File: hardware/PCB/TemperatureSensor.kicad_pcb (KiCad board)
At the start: 2 copper layers, 2 parts, among them IC1 BQ24092DGQR, IC2 ESP32-D0WD-V3

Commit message: Add new sensors to board
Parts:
- added IC3: SHT31-ARP-B2.5kS, ProjectFootprints:SON50P250X250X100-9N-D, F.Cu at (36.8, 22.9)
- added U1: LTR-329ALS-01, ProjectFootprints:LTR329ALS01, F.Cu at (59.7, 21.6)
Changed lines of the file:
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@@
     (tracks 0)
     (zones 0)
-    (modules 2)
+    (modules 4)
     (nets 1)
   )
@@
     (add_net "Net-(IC2-Pad8)")
     (add_net "Net-(IC2-Pad9)")
+    (add_net "Net-(IC3-Pad1)")
+    (add_net "Net-(IC3-Pad2)")
+    (add_net "Net-(IC3-Pad3)")
+    (add_net "Net-(IC3-Pad4)")
+    (add_net "Net-(IC3-Pad5)")
+    (add_net "Net-(IC3-Pad6)")
+    (add_net "Net-(IC3-Pad7)")
+    (add_net "Net-(IC3-Pad8)")
+    (add_net "Net-(IC3-Pad9)")
+    (add_net "Net-(U1-Pad1)")
+    (add_net "Net-(U1-Pad2)")
+    (add_net "Net-(U1-Pad3)")
+    (add_net "Net-(U1-Pad4)")
+  )
+  (module ProjectFootprints:LTR329ALS01 (layer F.Cu)
+    (at 59.69 21.59)
+    (descr LTR-329ALS-01)
+    (tags "Undefined or Miscellaneous")
+    (attr smd)
+    (fp_text reference U1 (at 0 0) (layer F.SilkS)
+      (effects (font (size 1.27 1.27) (thickness 0.254)))
+    )
+    (fp_text value LTR-329ALS-01 (at 0 0) (layer F.SilkS) hide
+      (effects (font (size 1.27 1.27) (thickness 0.254)))
+    )
+    (fp_arc (start -0.7 1.225) (end -0.6 1.225) (angle 180) (layer F.SilkS) (width 0.2))
+    (fp_arc (start -0.7 1.225) (end -0.8 1.225) (angle 180) (layer F.SilkS) (width 0.2))
+    (fp_text user %R (at 0 0) (layer F.Fab)
+      (effects (font (size 1.27 1.27) (thickness 0.254)))
+    )
+    (fp_line (start -1 -1.275) (end 1 -1.275) (layer F.Fab) (width 0.2))
+    (fp_line (start 1 -1.275) (end 1 0.725) (layer F.Fab) (width 0.2))
+    (fp_line (start 1 0.725) (end -1 0.725) (layer F.Fab) (width 0.2))
+    (fp_line (start -1 0.725) (end -1 -1.275) (layer F.Fab) (width 0.2))
+    (fp_line (start -1.5 -1.825) (end 1.5 -1.825) (layer F.CrtYd) (width 0.1))
+    (fp_line (start 1.5 -1.825) (end 1.5 1.825) (layer F.CrtYd) (width 0.1))
+    (fp_line (start 1.5 1.825) (end -1.5 1.825) (layer F.CrtYd) (width 0.1))
+    (fp_line (start -1.5 1.825) (end -1.5 -1.825) (layer F.CrtYd) (width 0.1))
+    (fp_line (start -0.1 -1.275) (end 0.1 -1.275) (layer F.SilkS) (width 0.1))
+    (fp_line (start -1 -0.375) (end -1 -0.175) (layer F.SilkS) (width 0.1))
+    (fp_line (start 1 -0.375) (end 1 -0.175) (layer F.SilkS) (width 0.1))
+    (fp_line (start -0.1 0.725) (end 0.1 0.725) (layer F.SilkS) (width 0.1))
+    (fp_line (start -0.8 1.225) (end -0.8 1.225) (layer F.SilkS) (width 0.2))
+    (fp_line (start -0.6 1.225) (end -0.6 1.225) (layer F.SilkS) (width 0.2))
+    (pad 4 smd rect (at -0.6 -0.95) (size 0.7 0.75) (layers F.Cu F.Paste F.Mask))
+    (pad 3 smd rect (at 0.6 -0.95) (size 0.7 0.75) (layers F.Cu F.Paste F.Mask))
+    (pad 2 smd rect (at 0.6 0.4) (size 0.7 0.75) (layers F.Cu F.Paste F.Mask))
+    (pad 1 smd rect (at -0.6 0.4) (size 0.7 0.75) (layers F.Cu F.Paste F.Mask))
+  )
+  (module ProjectFootprints:SON50P250X250X100-9N-D (layer F.Cu)
+    (at 36.83 22.86)
+    (descr "8-DFN (2.5x2.5)")
+    (tags "Integrated Circuit")
+    (attr smd)
+    (fp_text reference IC3 (at 0 0) (layer F.SilkS)
+      (effects (font (size 1.27 1.27) (thickness 0.254)))
+    )
+    (fp_text value SHT31-ARP-B2.5kS (at 0 0) (layer F.SilkS) hide
+      (effects (font (size 1.27 1.27) (thickness 0.254)))
+    )
+    (fp_text user %R (at 0 0) (layer F.Fab)
+      (effects (font (size 1.27 1.27) (thickness 0.254)))
+    )
+    (fp_line (start -1.85 -1.55) (end 1.85 -1.55) (layer F.CrtYd) (width 0.05))
+    (fp_line (start 1.85 -1.55) (end 1.85 1.55) (layer F.CrtYd) (width 0.05))
+    (fp_line (start 1.85 1.55) (end -1.85 1.55) (layer F.CrtYd) (width 0.05))
+    (fp_line (start -1.85 1.55) (end -1.85 -1.55) (layer F.CrtYd) (width 0.05))
+    (fp_line (start -1.25 -1.25) (end 1.25 -1.25) (layer F.Fab) (width 0.1))
+    (fp_line (start 1.25 -1.25) (end 1.25 1.25) (layer F.Fab) (width 0.1))
+    (fp_line (start 1.25 1.25) (end -1.25 1.25) (layer F.Fab) (width 0.1))
+    (fp_line (start -1.25 1.25) (end -1.25 -1.25) (layer F.Fab) (width 0.1))
+    (fp_line (start -1.25 -0.625) (end -0.625 -1.25) (layer F.Fab) (width 0.1))
+    (fp_circle (center -1.6 -1.4) (end -1.6 -1.275) (layer F.SilkS) (width 0.25))
+    (pad 9 smd rect (at 0 0) (size 1.2 1.9) (layers F.Cu F.Paste F.Mask))
+    (pad 8 smd rect (at 1.2 -0.75 90) (size 0.3 0.8) (layers F.Cu F.Paste F.Mask))
+    (pad 7 smd rect (at 1.2 -0.25 90) (size 0.3 0.8) (layers F.Cu F.Paste F.Mask))
+    (pad 6 smd rect (at 1.2 0.25 90) (size 0.3 0.8) (layers F.Cu F.Paste F.Mask))
+    (pad 5 smd rect (at 1.2 0.75 90) (size 0.3 0.8) (layers F.Cu F.Paste F.Mask))
+    (pad 4 smd rect (at -1.2 0.75 90) (size 0.3 0.8) (layers F.Cu F.Paste F.Mask))
+    (pad 3 smd rect (at -1.2 0.25 90) (size 0.3 0.8) (layers F.Cu F.Paste F.Mask))
+    (pad 2 smd rect (at -1.2 -0.25 90) (size 0.3 0.8) (layers F.Cu F.Paste F.Mask))
+    (pad 1 smd rect (at -1.2 -0.75 90) (size 0.3 0.8) (layers F.Cu F.Paste F.Mask))
+    (model C:\Users\Pascal\Documents\Projects\WeatherStation\hardware\Library\SamacSys_Parts.3dshapes\SHT31-ARP-B2.5kS.stp
+      (at (xyz 0 0 0))
+      (scale (xyz 1 1 1))
+      (rotate (xyz 0 0 0))
+    )
   )
   (module ProjectFootprints:QFN35P500X500X90-49N-D (layer F.Cu)

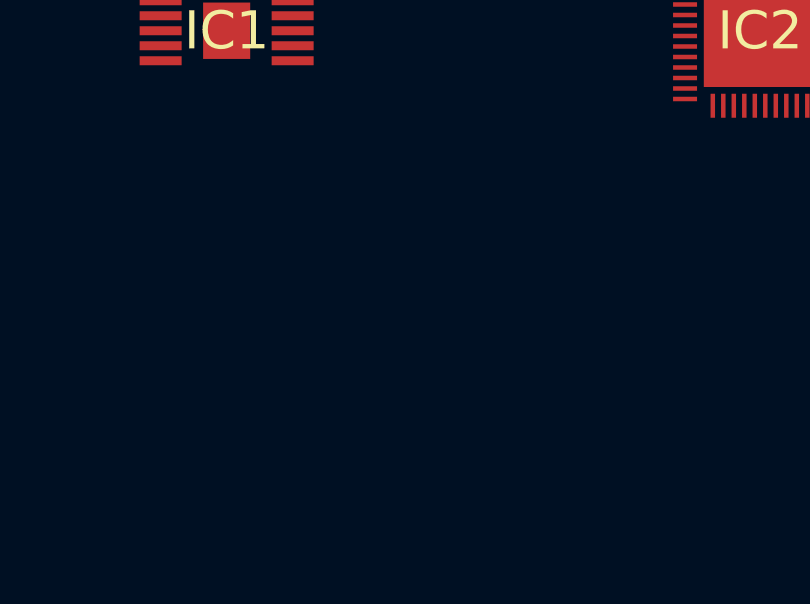
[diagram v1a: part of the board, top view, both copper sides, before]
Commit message: add usb and ftdi circuit
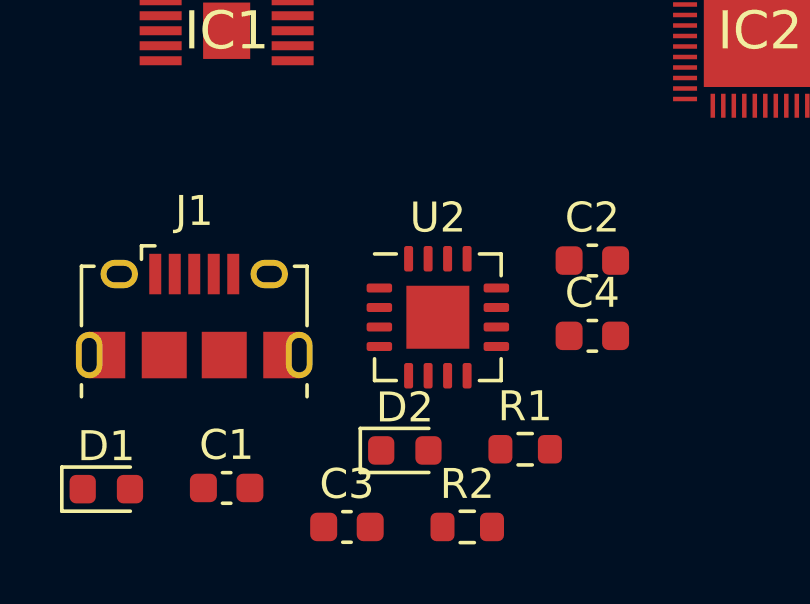
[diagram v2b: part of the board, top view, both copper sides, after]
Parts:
- added C1: 100n, Capacitor_SMD:C_0603_1608Metric, F.Cu at (31.8, 45.7)
- added C2: 4u7, Capacitor_SMD:C_0603_1608Metric, F.Cu at (43.9, 38.1)
- added C3: 100n, Capacitor_SMD:C_0603_1608Metric, F.Cu at (35.8, 47.0)
- added C4: 100n, Capacitor_SMD:C_0603_1608Metric, F.Cu at (43.9, 40.6)
- added D1: LED, LED_SMD:LED_0603_1608Metric, F.Cu at (27.7, 45.8)
- added D2: LED, LED_SMD:LED_0603_1608Metric, F.Cu at (37.7, 44.5)
- added J1: USB_B_Micro, Connector_USB:USB_Micro-B_Amphenol_10118194_Horizontal, F.Cu at (30.7, 40.0)
- added R1: 620R, Resistor_SMD:R_0603_1608Metric, F.Cu at (41.7, 44.4)
- added R2: 620R, Resistor_SMD:R_0603_1608Metric, F.Cu at (39.8, 47.0)
- added U2: FT230XQ, Package_DFN_QFN:QFN-16-1EP_4x4mm_P0.65mm_EP2.1x2.1mm, F.Cu at (38.8, 40.0)
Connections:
- IC1 pad 1: (no net) -> Net-(IC1-Pad1)
- IC1 pad 10: (no net) -> Net-(IC1-Pad10)
- IC1 pad 11: (no net) -> Net-(IC1-Pad11)
- IC1 pad 2: (no net) -> Net-(IC1-Pad2)
- IC1 pad 3: (no net) -> Net-(IC1-Pad3)
- IC1 pad 4: (no net) -> Net-(IC1-Pad4)
- IC1 pad 5: (no net) -> Net-(IC1-Pad5)
- IC1 pad 6: (no net) -> Net-(IC1-Pad6)
- IC1 pad 7: (no net) -> Net-(IC1-Pad7)
- IC1 pad 8: (no net) -> Net-(IC1-Pad8)
- IC1 pad 9: (no net) -> Net-(IC1-Pad9)
- IC2 pad 1: (no net) -> Net-(IC2-Pad1)
- IC2 pad 10: (no net) -> Net-(IC2-Pad10)
- IC2 pad 11: (no net) -> Net-(IC2-Pad11)
- IC2 pad 12: (no net) -> Net-(IC2-Pad12)
- IC2 pad 13: (no net) -> Net-(IC2-Pad13)
- IC2 pad 14: (no net) -> Net-(IC2-Pad14)
- IC2 pad 15: (no net) -> Net-(IC2-Pad15)
- IC2 pad 16: (no net) -> Net-(IC2-Pad16)
- IC2 pad 17: (no net) -> Net-(IC2-Pad17)
- IC2 pad 18: (no net) -> Net-(IC2-Pad18)
- IC2 pad 19: (no net) -> Net-(IC2-Pad19)
- IC2 pad 2: (no net) -> Net-(IC2-Pad2)
- IC2 pad 20: (no net) -> Net-(IC2-Pad20)
- IC2 pad 21: (no net) -> Net-(IC2-Pad21)
- IC2 pad 22: (no net) -> Net-(IC2-Pad22)
- IC2 pad 23: (no net) -> Net-(IC2-Pad23)
- IC2 pad 24: (no net) -> Net-(IC2-Pad24)
- IC2 pad 25: (no net) -> Net-(IC2-Pad25)
- IC2 pad 26: (no net) -> Net-(IC2-Pad26)
- IC2 pad 27: (no net) -> Net-(IC2-Pad27)
- IC2 pad 28: (no net) -> Net-(IC2-Pad28)
- IC2 pad 29: (no net) -> Net-(IC2-Pad29)
- IC2 pad 3: (no net) -> Net-(IC2-Pad3)
- IC2 pad 30: (no net) -> Net-(IC2-Pad30)
- IC2 pad 31: (no net) -> Net-(IC2-Pad31)
- IC2 pad 32: (no net) -> Net-(IC2-Pad32)
- IC2 pad 33: (no net) -> Net-(IC2-Pad33)
- IC2 pad 34: (no net) -> Net-(IC2-Pad34)
- IC2 pad 35: (no net) -> Net-(IC2-Pad35)
- IC2 pad 36: (no net) -> Net-(IC2-Pad36)
- IC2 pad 37: (no net) -> Net-(IC2-Pad37)
- IC2 pad 38: (no net) -> Net-(IC2-Pad38)
- IC2 pad 39: (no net) -> Net-(IC2-Pad39)
- IC2 pad 4: (no net) -> Net-(IC2-Pad4)
- IC2 pad 40: (no net) -> Net-(IC2-Pad40)
- IC2 pad 41: (no net) -> Net-(IC2-Pad41)
- IC2 pad 42: (no net) -> Net-(IC2-Pad42)
- IC2 pad 43: (no net) -> Net-(IC2-Pad43)
- IC2 pad 44: (no net) -> Net-(IC2-Pad44)
- IC2 pad 45: (no net) -> Net-(IC2-Pad45)
- IC2 pad 46: (no net) -> Net-(IC2-Pad46)
- IC2 pad 47: (no net) -> Net-(IC2-Pad47)
- IC2 pad 48: (no net) -> Net-(IC2-Pad48)
- IC2 pad 49: (no net) -> Net-(IC2-Pad49)
- IC2 pad 5: (no net) -> Net-(IC2-Pad5)
- IC2 pad 6: (no net) -> Net-(IC2-Pad6)
- IC2 pad 7: (no net) -> Net-(IC2-Pad7)
- IC2 pad 8: (no net) -> Net-(IC2-Pad8)
- IC2 pad 9: (no net) -> Net-(IC2-Pad9)
- IC3 pad 1: (no net) -> Net-(IC3-Pad1)
- IC3 pad 2: (no net) -> Net-(IC3-Pad2)
- IC3 pad 3: (no net) -> Net-(IC3-Pad3)
- IC3 pad 4: (no net) -> Net-(IC3-Pad4)
- IC3 pad 5: (no net) -> Net-(IC3-Pad5)
- IC3 pad 6: (no net) -> Net-(IC3-Pad6)
- IC3 pad 7: (no net) -> Net-(IC3-Pad7)
- IC3 pad 8: (no net) -> Net-(IC3-Pad8)
- IC3 pad 9: (no net) -> Net-(IC3-Pad9)
- U1 pad 1: (no net) -> Net-(U1-Pad1)
- U1 pad 2: (no net) -> Net-(U1-Pad2)
- U1 pad 3: (no net) -> Net-(U1-Pad3)
- U1 pad 4: (no net) -> Net-(U1-Pad4)

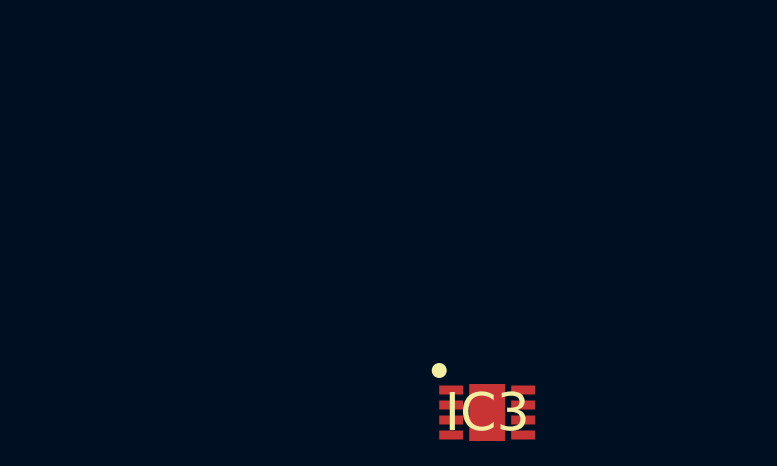
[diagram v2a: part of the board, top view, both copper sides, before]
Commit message: started display circuit
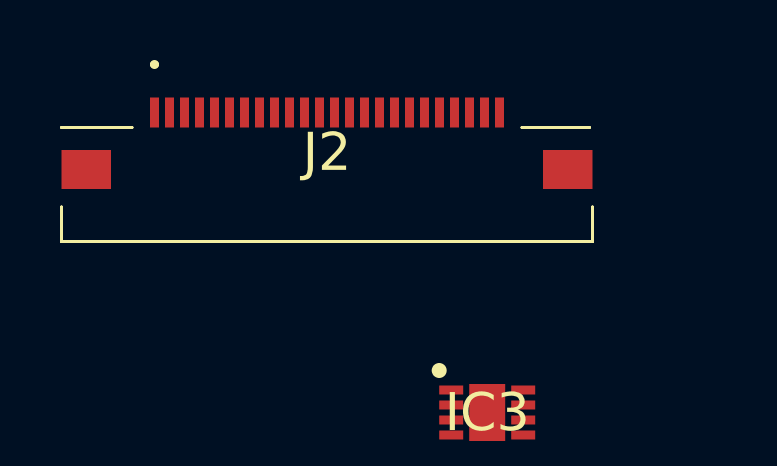
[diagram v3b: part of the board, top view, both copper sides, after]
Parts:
- added J2: 687124183622, ProjectFootprints:687124183622, F.Cu at (31.5, 15.3)

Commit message: updated pcb
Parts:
- added C1: 1u, Capacitor_SMD:C_0603_1608Metric, F.Cu at (94.0, 21.6)
- added C10: 1u, Capacitor_SMD:C_0603_1608Metric, F.Cu at (81.9, 30.4)
- added C11: 1u, Capacitor_SMD:C_0603_1608Metric, F.Cu at (85.9, 27.1)
- added C12: 1u, Capacitor_SMD:C_0603_1608Metric, F.Cu at (98.5, 18.8)
- added C13: 4u7, Capacitor_SMD:C_0603_1608Metric, F.Cu at (77.9, 27.9)
- added C14: 4u7, Capacitor_SMD:C_0603_1608Metric, F.Cu at (89.9, 27.1)
- added C15: 1u, Capacitor_SMD:C_0603_1608Metric, F.Cu at (120.8, 25.6)
- added C16: 4.7u, Capacitor_SMD:C_0603_1608Metric, F.Cu at (122.5, 22.6)
- added C17: 10u, Capacitor_SMD:C_0603_1608Metric, F.Cu at (128.3, 15.5)
- added C18: 10u, Capacitor_SMD:C_0603_1608Metric, F.Cu at (122.5, 20.1)
- added C19: 100n, Capacitor_SMD:C_0603_1608Metric, F.Cu at (150.2, 15.5)
- added C2: 1u, Capacitor_SMD:C_0603_1608Metric, F.Cu at (85.9, 29.6)
- added C20: 1u, Capacitor_SMD:C_0603_1608Metric, F.Cu at (143.3, 21.1)
- added C21: TBD, Capacitor_SMD:C_0603_1608Metric, F.Cu at (114.5, 45.7)
- added C22: 10u, Capacitor_SMD:C_0603_1608Metric, F.Cu at (126.6, 43.7)
- added C23: 1u, Capacitor_SMD:C_0603_1608Metric, F.Cu at (118.5, 43.2)
- added C24: 100n, Capacitor_SMD:C_0603_1608Metric, F.Cu at (123.9, 38.6)
- added C25: TBD, Capacitor_SMD:C_0603_1608Metric, F.Cu at (123.9, 36.1)
- added C26: 100n, Capacitor_SMD:C_0603_1608Metric, F.Cu at (127.9, 36.1)
- added C27: 100n, Capacitor_SMD:C_0603_1608Metric, F.Cu at (114.5, 48.2)
- added C28: 3n3, Capacitor_SMD:C_0603_1608Metric, F.Cu at (123.9, 41.1)
- added C29: 10n, Capacitor_SMD:C_0603_1608Metric, F.Cu at (130.6, 43.7)
- added C3: 100n, Capacitor_SMD:C_0603_1608Metric, F.Cu at (154.2, 15.5)
- added C30: 100n, Capacitor_SMD:C_0603_1608Metric, F.Cu at (122.6, 46.2)
- added C31: 100n, Capacitor_SMD:C_0603_1608Metric, F.Cu at (127.9, 41.1)
- added C32: 100n, Capacitor_SMD:C_0603_1608Metric, F.Cu at (122.6, 43.7)
- added C33: 100n, Capacitor_SMD:C_0603_1608Metric, F.Cu at (118.5, 48.2)
- added C34: 100n, Capacitor_SMD:C_0603_1608Metric, F.Cu at (154.3, 37.1)
- added C35: 4u7, Capacitor_SMD:C_0603_1608Metric, F.Cu at (146.1, 43.5)
- added C36: 100n, Capacitor_SMD:C_0603_1608Metric, F.Cu at (154.3, 34.6)
- added C37: 100n, Capacitor_SMD:C_0603_1608Metric, F.Cu at (142.1, 42.2)
- added C38: 12p5, Capacitor_SMD:C_0603_1608Metric, F.Cu at (127.9, 38.6)
- added C39: 12p5, Capacitor_SMD:C_0603_1608Metric, F.Cu at (118.5, 45.7)
- added C4: 100n, Capacitor_SMD:C_0603_1608Metric, F.Cu at (147.4, 19.6)
- added C40: 4p, Capacitor_SMD:C_0603_1608Metric, F.Cu at (115.6, 81.3)
- added C41: 4p, Capacitor_SMD:C_0603_1608Metric, F.Cu at (124.6, 78.6)
- added C42: 100n, Capacitor_SMD:C_0603_1608Metric, F.Cu at (119.6, 81.3)
- added C43: 100n, Capacitor_SMD:C_0603_1608Metric, F.Cu at (129.5, 74.0)
- added C44: 100n, Capacitor_SMD:C_0603_1608Metric, F.Cu at (134.9, 68.7)
- added C5: 1u, Capacitor_SMD:C_0603_1608Metric, F.Cu at (81.9, 27.9)
- added C6: 1u, Capacitor_SMD:C_0603_1608Metric, F.Cu at (99.7, 15.5)
- added C7: 1u, Capacitor_SMD:C_0603_1608Metric, F.Cu at (77.9, 30.4)
- added C8: 1u, Capacitor_SMD:C_0603_1608Metric, F.Cu at (84.7, 24.5)
- added C9: 1u, Capacitor_SMD:C_0603_1608Metric, F.Cu at (88.7, 24.5)
- added D1: LED, LED_SMD:LED_0603_1608Metric, F.Cu at (138.1, 42.3)
- added D2: LED, LED_SMD:LED_0603_1608Metric, F.Cu at (148.1, 41.0)
- added D3: MBR0530, Diode_SMD:D_SOD-123, F.Cu at (79.8, 25.0)
- added D4: MBR0530, Diode_SMD:D_SOD-123, F.Cu at (74.0, 25.0)
- added D5: MBR0530, Diode_SMD:D_SOD-123, F.Cu at (94.8, 15.9)
- added H1: MountingHole_Pad, MountingHole:MountingHole_3.2mm_M3_Pad_Via, F.Cu at (83.1, 46.8)
- added H2: MountingHole_Pad, MountingHole:MountingHole_3.2mm_M3_Pad_Via, F.Cu at (75.2, 38.9)
- added H3: MountingHole_Pad, MountingHole:MountingHole_3.2mm_M3_Pad_Via, F.Cu at (83.1, 38.9)
- added H4: MountingHole_Pad, MountingHole:MountingHole_3.2mm_M3_Pad_Via, F.Cu at (75.2, 46.8)
- added IC1: BQ24092DGQR, ProjectFootprints:SOP50P490X110-11N, F.Cu at (118.2, 16.6)
- added IC2: SHT30-DIS-B2.5KS, ProjectFootprints:SHT30DISB25KS, F.Cu at (140.6, 17.0)
- added IC3: LPS22HDTR, ProjectFootprints:LPS22HDTR, F.Cu at (146.1, 16.3)
- added IC4: TPS62291DRVR, ProjectFootprints:SON65P200X200X80-7N, F.Cu at (116.6, 26.4)
- added IC5: ESP32-D0WD-V3, ProjectFootprints:QFN35P500X500X90-49N-D, F.Cu at (108.9, 45.6)
- added J1: USB_B_Micro, Connector_USB:USB_Micro-B_Amphenol_10118194_Horizontal, F.Cu at (141.0, 36.5)
- added J2: 687124183622, ProjectFootprints:687124183622, F.Cu at (81.6, 19.8)
- added J3: S2B-XH-A_LF__SN_, ProjectFootprints:SHDRRA2W80P0X250_1X2_740X1150X610P, F.Cu at (108.8, 24.2)
- added L1: 68u, Inductor_SMD:L_0805_2012Metric, F.Cu at (94.2, 19.0)
- added L2: 2.2u, Inductor_SMD:L_Coilcraft_LPS4018, F.Cu at (117.5, 21.6)
- added L3: 0R, Inductor_SMD:L_0603_1608Metric, F.Cu at (122.6, 48.7)
- added L4: 2n, Inductor_SMD:L_0603_1608Metric, F.Cu at (126.6, 46.2)
- added LED1: SML-D12Y1WT86, ProjectFootprints:LEDC1608X55N, F.Cu at (107.8, 28.7)
- added LED2: SML-D12Y1WT86, ProjectFootprints:LEDC1608X55N, F.Cu at (124.1, 15.7)
- added Q1: SI1308EDL-T1-BE3, ProjectFootprints:SOT65P210X110-3N, F.Cu at (73.5, 28.5)
- added Q2: SS8050-G, ProjectFootprints:SOT95P240X115-3N, F.Cu at (125.1, 75.0)
- added Q3: SS8050-G, ProjectFootprints:SOT95P240X115-3N, F.Cu at (130.5, 69.7)
- added R1: 10k, Resistor_SMD:R_0603_1608Metric, F.Cu at (128.3, 18.0)
- added R10: 2.2k, Resistor_SMD:R_0603_1608Metric, F.Cu at (120.8, 28.1)
- added R11: 120, Resistor_SMD:R_0603_1608Metric, F.Cu at (126.5, 20.5)
- added R12: 120, Resistor_SMD:R_0603_1608Metric, F.Cu at (112.0, 28.5)
- added R13: 10k, Resistor_SMD:R_0603_1608Metric, F.Cu at (147.4, 22.1)
- added R14: 10k, Resistor_SMD:R_0603_1608Metric, F.Cu at (151.4, 18.0)
- added R15: 10k, Resistor_SMD:R_0603_1608Metric, F.Cu at (151.4, 20.5)
- added R16: 10k, Resistor_SMD:R_0603_1608Metric, F.Cu at (147.4, 24.6)
- added R17: 20k, Resistor_SMD:R_0603_1608Metric, F.Cu at (114.5, 43.2)
- added R18: 620R, Resistor_SMD:R_0603_1608Metric, F.Cu at (152.1, 40.9)
- added R19: 620R, Resistor_SMD:R_0603_1608Metric, F.Cu at (150.1, 43.5)
- added R2: 10k, Resistor_SMD:R_0603_1608Metric, F.Cu at (143.3, 23.6)
- added R20: 10k, Resistor_SMD:R_0603_1608Metric, F.Cu at (124.6, 81.1)
- added R21: 10k, Resistor_SMD:R_0603_1608Metric, F.Cu at (128.7, 78.6)
- added R22: 10k, Resistor_SMD:R_0603_1608Metric, F.Cu at (134.9, 71.2)
- added R23: 10k, Resistor_SMD:R_0603_1608Metric, F.Cu at (133.5, 73.7)
- added R3: 10k, Resistor_SMD:R_0603_1608Metric, F.Cu at (92.7, 24.5)
- added R4: 10k, Resistor_SMD:R_0603_1608Metric, F.Cu at (98.0, 21.6)
- added R5: 10k, Resistor_SMD:R_0603_1608Metric, F.Cu at (89.9, 29.6)
- added R6: 10k, Resistor_SMD:R_0603_1608Metric, F.Cu at (96.7, 24.1)
- added R7: 10k, Resistor_SMD:R_0603_1608Metric, F.Cu at (93.9, 27.1)
- added R8: 3R0, Resistor_SMD:R_0603_1608Metric, F.Cu at (93.9, 29.6)
- added R9: 680, Resistor_SMD:R_0603_1608Metric, F.Cu at (124.8, 25.2)
- added S1: PTS815_SJM_250_SMTR_LFS, ProjectFootprints:PTS815SJM250SMTRLFS, F.Cu at (118.3, 70.6)
- added S2: PTS815_SJM_250_SMTR_LFS, ProjectFootprints:PTS815SJM250SMTRLFS, F.Cu at (118.3, 76.9)
- added U1: LTR-329ALS-01, ProjectFootprints:LTR329ALS01, F.Cu at (139.3, 22.2)
- added U2: FT231XQ, Package_DFN_QFN:QFN-20-1EP_4x4mm_P0.5mm_EP2.5x2.5mm, F.Cu at (146.6, 70.5)
- added U2: FT230XQ, Package_DFN_QFN:QFN-16-1EP_4x4mm_P0.65mm_EP2.1x2.1mm, F.Cu at (149.2, 36.5)
- added U3: ESP32_Antenna, RF_Antenna:Texas_SWRA117D_2.4GHz_Right, F.Cu at (109.0, 41.0)
- added Y1: ABS05-32.768KHZ-T, ProjectFootprints:ABS05, F.Cu at (126.4, 48.5)
- added Y2: ABM11AIG-40.000MHZ-4-1Z-T, ProjectFootprints:ABM11AIG40000MHZ41ZT, F.Cu at (125.3, 69.9)
